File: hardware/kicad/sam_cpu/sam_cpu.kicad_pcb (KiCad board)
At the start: 2 copper layers, 142 x 231.8 mm, 465 parts, among them J1 J1 SWITCH COLUMNS, J10 J10 SPEAKERS, J11 J11 POWER, J12 J12 SWITCH ROWS, J13 J13 DEDICATED, J17 EXT 5V, J18 J18 GI DIMMER, J19 USB-C (to Pi), J2 J2 DEDICATED, J20 SWD, J21 Raspberry Pi 40-pin, J22 J22 STEREO, J23 EXT 12V, J24 J24 SUBWOOFER, J25 J25 HUB75 PANEL A, J26 J26 HUB75 PANEL B, J3 J3 DEDICATED, J5 J5 DMD, J6 J6 SWITCH ROWS, J9 J9 IO BUS, Q1 AO3401A, Q11 MMBT3904, Q12 MMBT3904, Q13 MMBT3904, Q14 MMBT3904, Q15 MMBT3904, Q16 MMBT3904, Q17 MMBT3904, Q18 MMBT3904, Q2 AO3401A, Q3 2N7002, Q4 2N7002, SW1 RESET, SW2 BOOTSEL, SW3 DIP x8, U1 LTC4412, U10 LM339, U11 LM339, U14 74HC165, U15 74HC165, U16 74HC165, U17 74HC165, U18 74HC165, U19 74HC165, U2 LTC4412, U20 74HC595, U21 74HCT245, U22 PCM5102A, U23 TDA7297, U24 TDA7297, U25 DS3231MZ, U26 OPA1678, U27 74AHCT245, U28 74AHCT245, U29 74AHCT245, U3 NCP1117-3.3, U30 74HC165, U31 74HC595, U4 RP2354B, U5 TPS3808G33, U6 SN74LVC8T245, U7 74AHCT541, U8 LM339, U9 LM339, Y1 12MHz

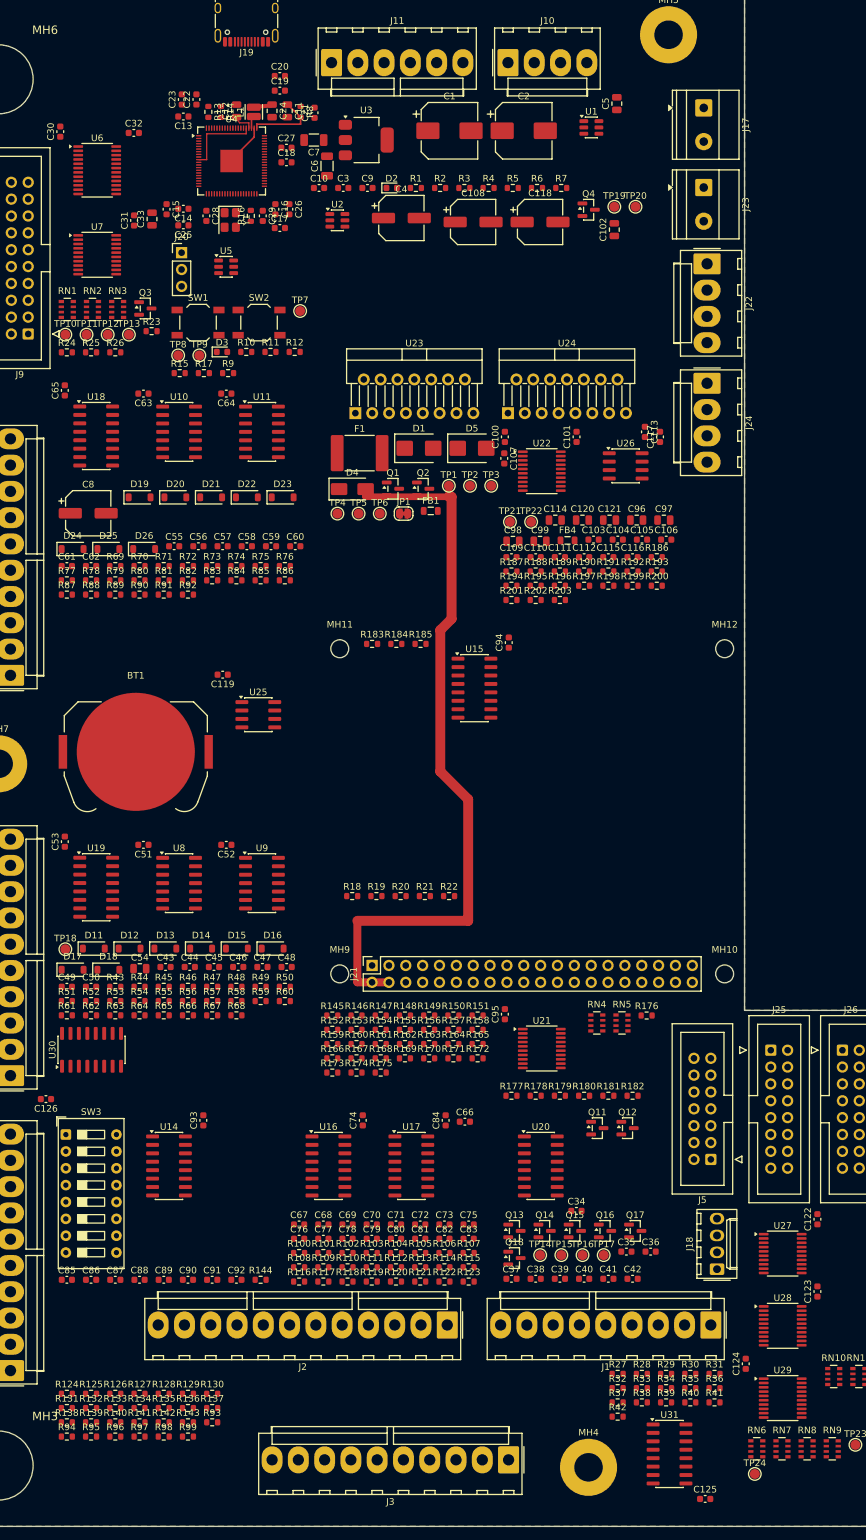
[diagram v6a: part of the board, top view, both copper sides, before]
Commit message: Layout: ground via per SMD ground pad, 3x3 vias under the RP2354B pad
tools/changes/c07_gnd_fanout.py gives each of the 256 SMD GND pads a locked
0.3 mm stub and via so they reach the bottom pour, plus a 3x3 array in the
RP2354B exposed pad. tools/changes/route/ holds the Freerouting helpers
(GND dropped from the routing netlist, its copper passed as keepouts).

Co-Authored-By: Claude Opus 5.5 (1M context) <noreply@anthropic.com>
Claude-Session: https://claude.ai/code/session_01ExuDVoDDDHhVWjb8EwVzYb
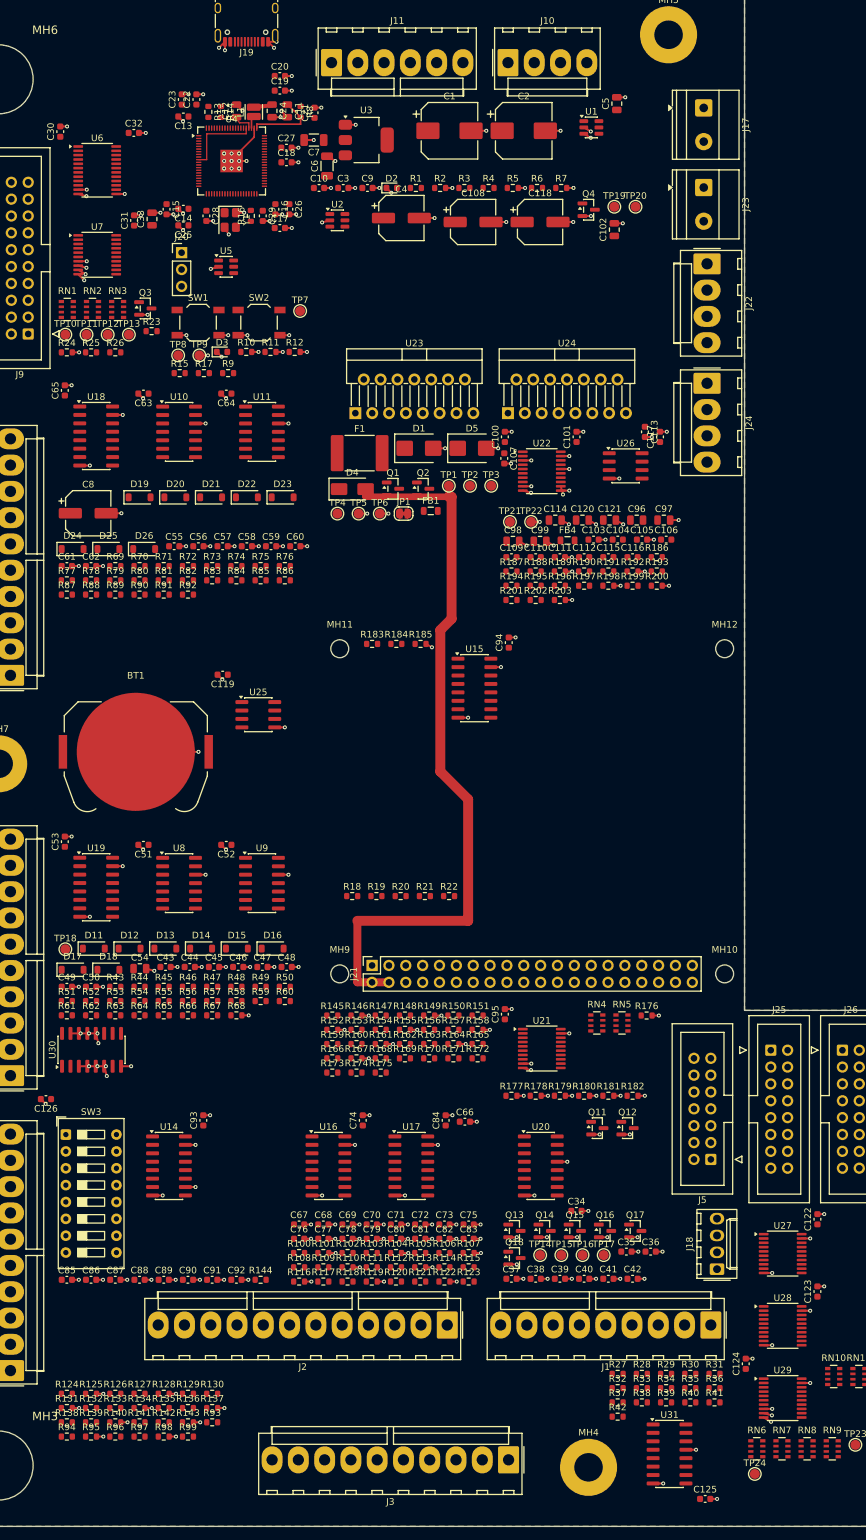
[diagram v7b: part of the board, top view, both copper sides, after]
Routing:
- net GND: track 4.25 -> 320.1 mm, vias 0 -> 265
